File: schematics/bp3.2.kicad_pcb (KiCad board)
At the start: 2 copper layers, 69.5 x 25 mm, 56 parts, among them J1 PowerInput, J2 PowerPassThru, J3 OutputPins, U1 INA128, U2 INA128, U3 INA128, U4 INA128

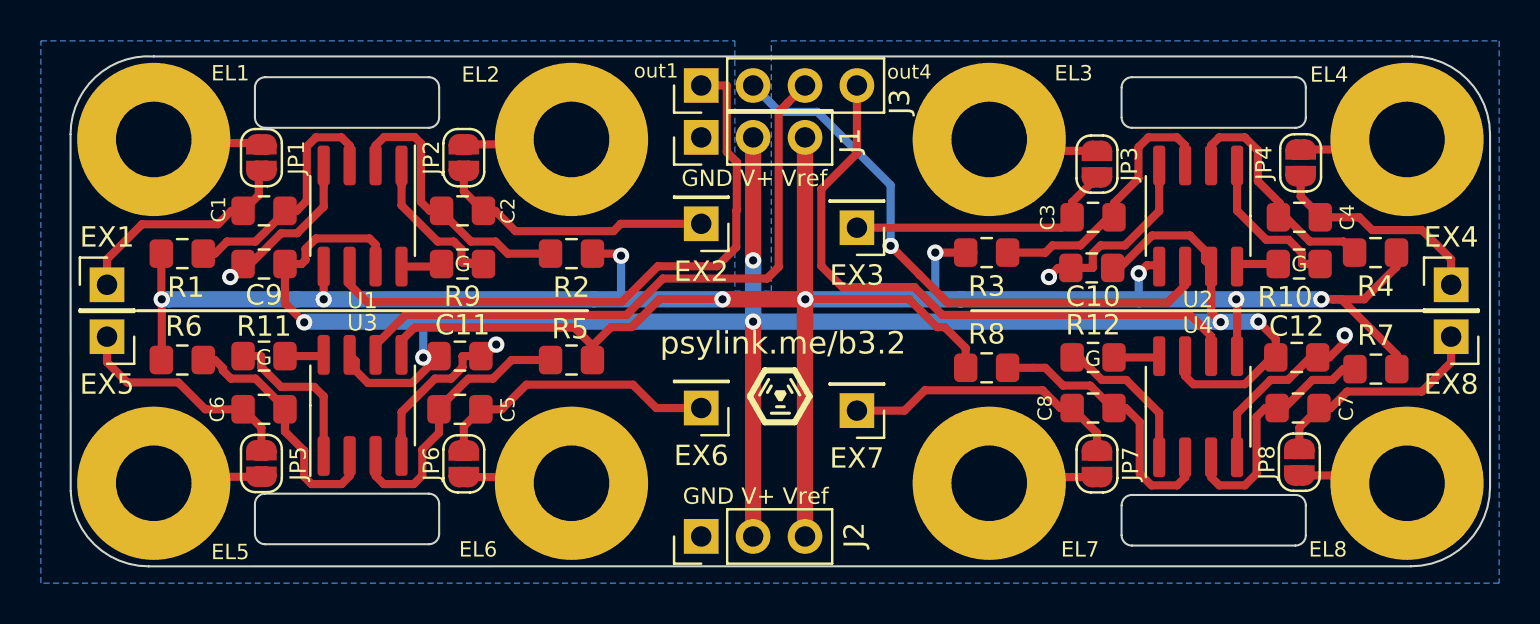
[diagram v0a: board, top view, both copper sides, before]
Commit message: draw rectangles around gain resistors
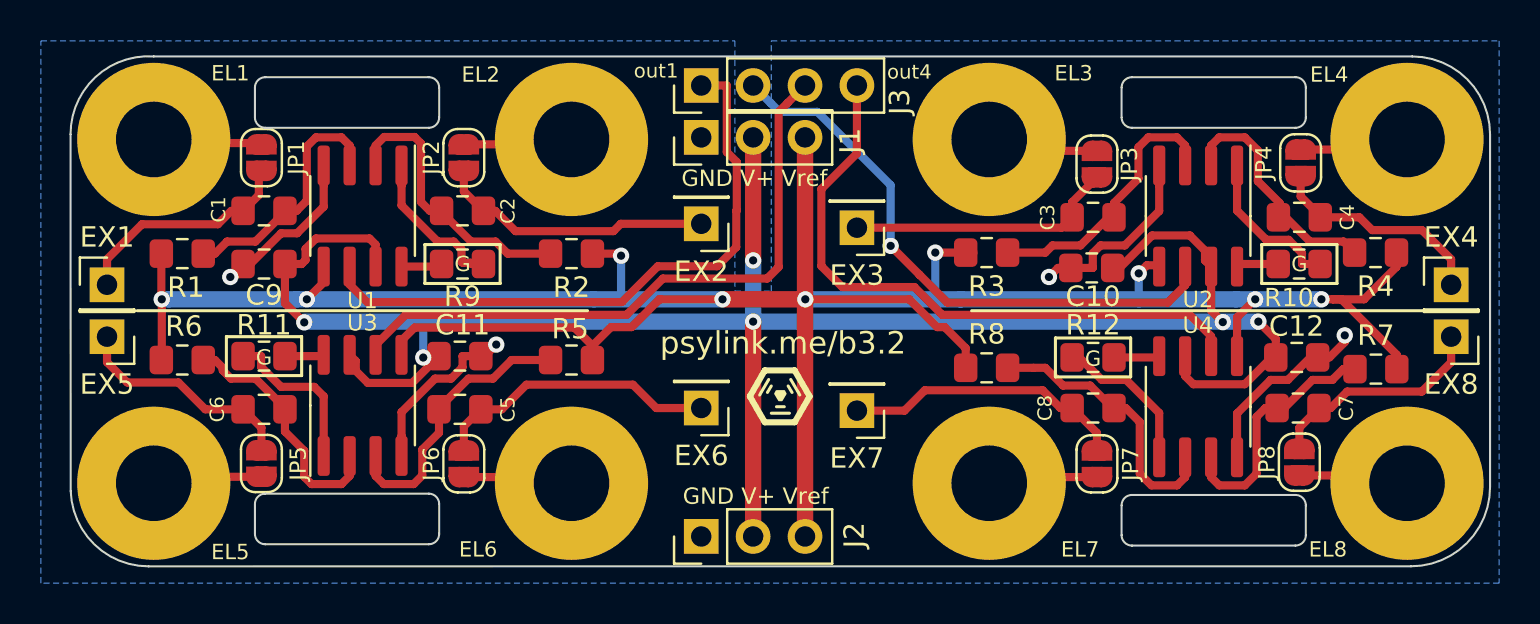
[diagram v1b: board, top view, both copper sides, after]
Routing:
- net GNDS: track 134.4 -> 135.0 mm
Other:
- board text added: "rectangles indicate gain resistors"
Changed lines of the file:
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@@
   (general
     (thickness 1.6)
-    (drawings 70)
-    (tracks 397)
+    (drawings 91)
+    (tracks 398)
     (zones 0)
     (modules 56)
@@
     (tags "resistor handsolder")
     (attr smd)
-    (fp_text reference R10 (at 0.6895 -1.6129) (layer F.SilkS)
-      (effects (font (size 1 1) (thickness 0.15)))
+    (fp_text reference R10 (at 0.499 -1.651) (layer F.SilkS)
+      (effects (font (size 0.9 0.9) (thickness 0.15)))
     )
     (fp_text value 1K/1% (at 0 1.65) (layer F.Fab)
@@
     (tags "resistor handsolder")
     (attr smd)
-    (fp_text reference R11 (at 0 -1.4605 180) (layer F.SilkS)
+    (fp_text reference R11 (at 0 -1.524 180) (layer F.SilkS)
       (effects (font (size 1 1) (thickness 0.15)))
     )
@@
       ))
   )
+  (gr_line (start 82.4865 35.7505) (end 25.019 41.2115) (layer Cmts.User) (width 0.15))
+  (gr_line (start 72.9615 40.767) (end 25.146 41.5925) (layer Cmts.User) (width 0.15))
+  (gr_line (start 42.545 36.2585) (end 24.0665 40.513) (layer Cmts.User) (width 0.15))
+  (gr_line (start 32.8295 39.8145) (end 23.8125 41.021) (layer Cmts.User) (width 0.15))
+  (gr_text "rectangles\nindicate gain\nresistors" (at 17.8435 42.164) (layer Cmts.User)
+    (effects (font (size 1 1) (thickness 0.15)))
+  )
+  (gr_line (start 83.693 34.6075) (end 87.376 34.6075) (layer F.SilkS) (width 0.15))
+  (gr_line (start 87.376 36.5125) (end 83.693 36.5125) (layer F.SilkS) (width 0.15))
+  (gr_line (start 83.693 36.5125) (end 83.693 34.6075) (layer F.SilkS) (width 0.15))
+  (gr_line (start 87.376 34.6075) (end 87.376 36.5125) (layer F.SilkS) (width 0.15))
+  (gr_line (start 73.5965 39.1795) (end 77.2795 39.1795) (layer F.SilkS) (width 0.15))
+  (gr_line (start 77.2795 41.0845) (end 73.5965 41.0845) (layer F.SilkS) (width 0.15))
+  (gr_line (start 73.5965 41.0845) (end 73.5965 39.1795) (layer F.SilkS) (width 0.15))
+  (gr_line (start 77.2795 39.1795) (end 77.2795 41.0845) (layer F.SilkS) (width 0.15))
+  (gr_line (start 42.7355 34.6075) (end 46.4185 34.6075) (layer F.SilkS) (width 0.15))
+  (gr_line (start 46.4185 36.5125) (end 42.7355 36.5125) (layer F.SilkS) (width 0.15))
+  (gr_line (start 42.7355 36.5125) (end 42.7355 34.6075) (layer F.SilkS) (width 0.15))
+  (gr_line (start 46.4185 34.6075) (end 46.4185 36.5125) (layer F.SilkS) (width 0.15))
+  (gr_line (start 33.02 41.021) (end 33.02 39.116) (layer F.SilkS) (width 0.15))
+  (gr_line (start 36.703 41.021) (end 33.02 41.021) (layer F.SilkS) (width 0.15))
+  (gr_line (start 36.703 39.116) (end 36.703 41.021) (layer F.SilkS) (width 0.15))
+  (gr_line (start 33.02 39.116) (end 36.703 39.116) (layer F.SilkS) (width 0.15))
   (gr_line (start 59.69 42.8625) (end 60.579 42.8625) (layer F.SilkS) (width 0.15))
   (gr_line (start 59.944 42.545) (end 60.325 42.545) (layer F.SilkS) (width 0.15))
@@
   (gr_line (start 60.833 40.767) (end 61.563678 42.030839) (layer F.SilkS) (width 0.3))
   (gr_line (start 59.3725 40.767) (end 60.833 40.767) (layer F.SilkS) (width 0.3))
-  (gr_text "This hole in\nthe fill area\nbreaks the\nground loop" (at 19.304 34.3027) (layer Cmts.User)
+  (gr_text "This hole in\nthe fill area\nbreaks the\nground loop" (at 59.055 20.701) (layer Cmts.User)
     (effects (font (size 1 1) (thickness 0.15)))
   )
@@
   (segment (start 58.801 29.3624) (end 58.8264 29.3624) (width 0.8) (layer B.Cu) (net 18))
   (segment (start 58.801 38.3794) (end 58.801 38.3794) (width 0.8) (layer B.Cu) (net 18))
-  (segment (start 81.2165 35.622) (end 81.2165 37.9349) (width 0.4) (layer F.Cu) (net 18))
-  (segment (start 81.2165 37.9349) (end 81.6864 38.4048) (width 0.4) (layer F.Cu) (net 18))
-  (via (at 81.6864 38.4048) (size 0.8) (drill 0.4) (layers F.Cu B.Cu) (net 18))
+  (via (at 81.788 38.4048) (size 0.8) (drill 0.4) (layers F.Cu B.Cu) (net 18))
   (segment (start 58.801 38.3794) (end 45.6184 38.3794) (width 0.8) (layer B.Cu) (net 18))
   (via (at 58.801 38.3794) (size 0.8) (drill 0.4) (layers F.Cu B.Cu) (net 18))
@@
   (segment (start 84.3825 40.132) (end 84.3825 39.234) (width 0.4) (layer F.Cu) (net 18))
   (segment (start 58.801 38.3794) (end 83.5279 38.3794) (width 0.8) (layer B.Cu) (net 18))
+  (segment (start 81.2165 37.8333) (end 81.788 38.4048) (width 0.4) (layer F.Cu) (net 18))
+  (segment (start 81.2165 35.6855) (end 81.2165 37.8333) (width 0.4) (layer F.Cu) (net 18))
   (segment (start 57.3024 37.2872) (end 57.3024 37.2872) (width 0.8) (layer F.Cu) (net 19))
   (via (at 57.3024 37.2872) (size 0.8) (drill 0.4) (layers F.Cu B.Cu) (net 19))
@@
   (via (at 77.6732 36.0172) (size 0.8) (drill 0.4) (layers F.Cu B.Cu) (net 19))
   (segment (start 82.4484 37.2872) (end 86.614 37.2872) (width 0.8) (layer B.Cu) (net 19))
-  (via (at 82.4484 37.2872) (size 0.8) (drill 0.4) (layers F.Cu B.Cu) (net 19))
-  (segment (start 82.4865 37.3253) (end 82.4484 37.2872) (width 0.4) (layer F.Cu) (net 19))
-  (segment (start 82.4865 40.07) (end 82.4865 37.3253) (width 0.4) (layer F.Cu) (net 19))
+  (via (at 83.3755 37.2872) (size 0.8) (drill 0.4) (layers F.Cu B.Cu) (net 19))
   (segment (start 68.9864 37.2872) (end 77.6732 37.2872) (width 0.8) (layer B.Cu) (net 19))
   (segment (start 77.6732 37.2872) (end 77.6732 36.0172) (width 0.4) (layer B.Cu) (net 19))
   (segment (start 77.6732 37.2872) (end 82.4484 37.2872) (width 0.8) (layer B.Cu) (net 19))
-  (segment (start 37.7825 35.622) (end 37.7825 37.2872) (width 0.4) (layer F.Cu) (net 19))
-  (via (at 37.7825 37.2872) (size 0.8) (drill 0.4) (layers F.Cu B.Cu) (net 19))
+  (via (at 36.957 37.2872) (size 0.8) (drill 0.4) (layers F.Cu B.Cu) (net 19))
   (segment (start 61.341 29.3624) (end 61.341 48.895) (width 0.8) (layer F.Cu) (net 19))
   (segment (start 61.3537 37.2872) (end 66.4464 37.2872) (width 0.4) (layer F.Cu) (net 19))
@@
   (segment (start 52.2351 35.052) (end 52.3367 35.1536) (width 0.4) (layer F.Cu) (net 19))
   (segment (start 50.936 35.052) (end 52.2351 35.052) (width 0.4) (layer F.Cu) (net 19))
+  (segment (start 37.7825 36.4617) (end 36.957 37.2872) (width 0.4) (layer F.Cu) (net 19))
+  (segment (start 37.7825 35.6855) (end 37.7825 36.4617) (width 0.4) (layer F.Cu) (net 19))
+  (segment (start 82.4865 38.1762) (end 83.3755 37.2872) (width 0.4) (layer F.Cu) (net 19))
+  (segment (start 82.4865 40.07) (end 82.4865 38.1762) (width 0.4) (layer F.Cu) (net 19))
   (segment (start 57.511001 30.079001) (end 57.511 26.8224) (width 0.4) (layer F.Cu) (net 20))
   (segment (start 57.511 26.8224) (end 56.261 26.8224) (width 0.4) (layer F.Cu) (net 20))

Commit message: hide U* labels under chips. add "signal*" labels.
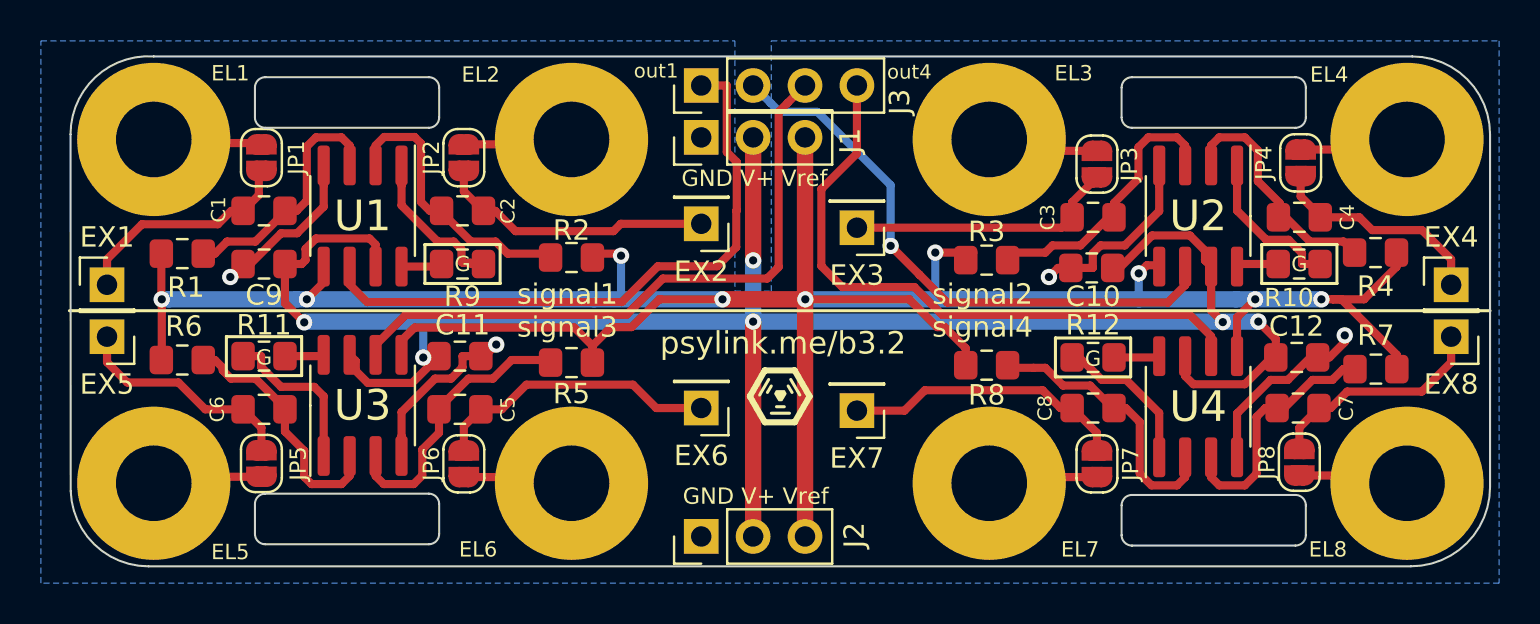
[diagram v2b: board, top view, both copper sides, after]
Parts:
- moved R3 0.37 mm to (70.2, 35.4)
- moved R2 0.19 mm to (49.9, 35.2)
- moved R5 0.13 mm to (49.9, 40.4)
- moved R8 0.13 mm to (70.2, 40.5)
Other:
- board text added: "signal1 signal3"
- board text added: "signal2 signal4"

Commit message: grow INA128's solder pads for easier assembly
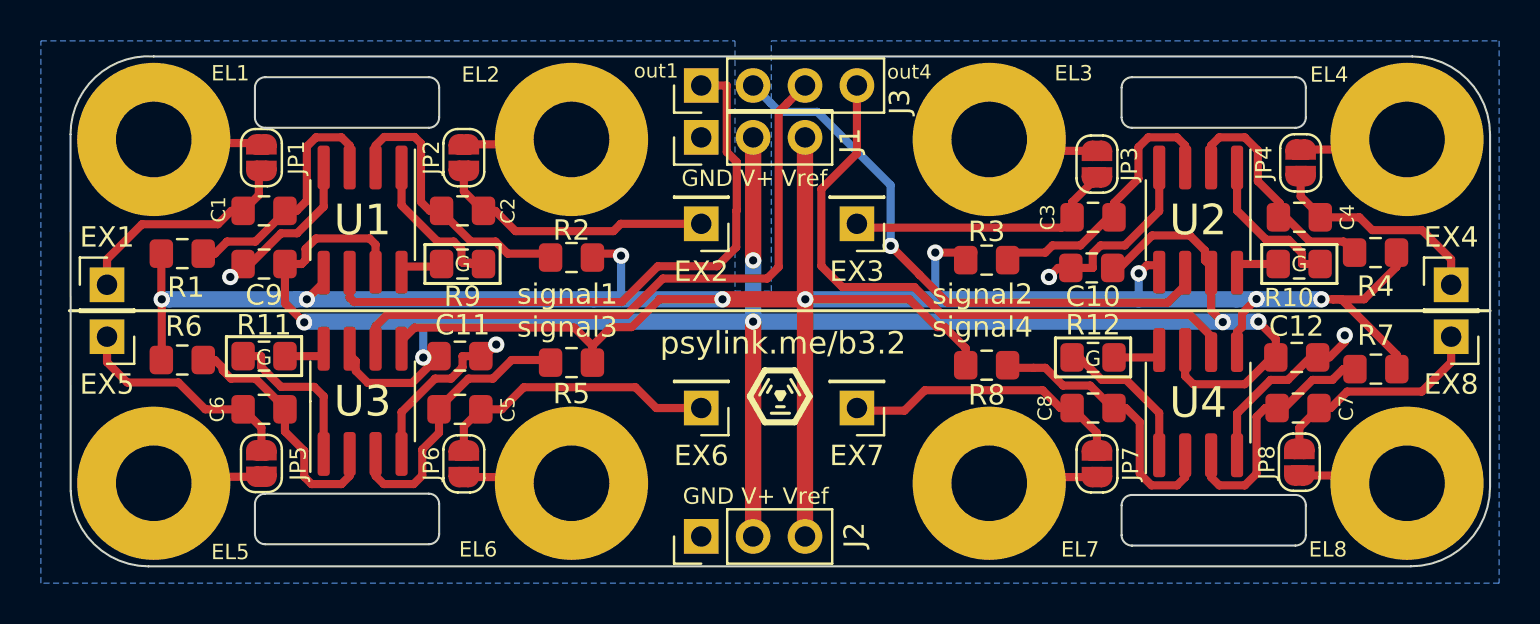
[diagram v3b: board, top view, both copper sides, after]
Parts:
- moved U4 0.20 mm to (80.6, 42.3)
- moved U1 0.20 mm to (39.7, 33.4)
- moved U2 0.20 mm to (80.6, 33.4)
- moved U3 0.20 mm to (39.7, 42.3)
- moved EX3 0.19 mm to (63.9, 33.6)
- moved EX7 0.13 mm to (63.9, 42.6)
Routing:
- net /out1: track 30.8 -> 31.8 mm
- net /out3: track 31.2 -> 32.0 mm

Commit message: tweak silkscreen
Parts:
- J1, J2, J3: moved to B.Cu
- turned J1 to 270 degrees
- turned J2 to 270 degrees
- turned J3 to 270 degrees

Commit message: add silkscreen on backside for signals and electrode polarity
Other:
- board text added: "+"
- board text added: "-"
- board text added: "signal 1"
- board text added: "signal 2"
- board text added: "signal 3"
- board text added: "signal 4"
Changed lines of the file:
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@@
   (general
     (thickness 1.6)
-    (drawings 92)
+    (drawings 108)
     (tracks 402)
     (zones 0)
@@
       ))
   )
+  (gr_text - (at 49.911 41.402) (layer B.SilkS)
+    (effects (font (size 1 1) (thickness 0.15)) (justify mirror))
+  )
+  (gr_text + (at 70.358 41.402) (layer B.SilkS)
+    (effects (font (size 1 1) (thickness 0.15)) (justify mirror))
+  )
+  (gr_text - (at 90.805 41.402) (layer B.SilkS)
+    (effects (font (size 1 1) (thickness 0.15)) (justify mirror))
+  )
+  (gr_text + (at 29.464 41.402) (layer B.SilkS)
+    (effects (font (size 1 1) (thickness 0.15)) (justify mirror))
+  )
+  (gr_text + (at 90.805 34.163) (layer B.SilkS)
+    (effects (font (size 1 1) (thickness 0.15)) (justify mirror))
+  )
+  (gr_text - (at 70.358 34.163) (layer B.SilkS)
+    (effects (font (size 1 1) (thickness 0.15)) (justify mirror))
+  )
+  (gr_text - (at 29.464 34.163) (layer B.SilkS)
+    (effects (font (size 1 1) (thickness 0.15)) (justify mirror))
+  )
+  (gr_text + (at 49.911 34.163) (layer B.SilkS)
+    (effects (font (size 1 1) (thickness 0.15)) (justify mirror))
+  )
+  (gr_text "signal 4" (at 78.1685 44.1325) (layer B.SilkS)
+    (effects (font (size 1 1) (thickness 0.15)) (justify mirror))
+  )
+  (gr_line (start 73.914 44.831) (end 87.249 44.831) (layer B.SilkS) (width 0.15))
+  (gr_line (start 73.914 30.988) (end 87.249 30.988) (layer B.SilkS) (width 0.15))
+  (gr_text "signal 2" (at 78.1685 30.2895) (layer B.SilkS)
+    (effects (font (size 1 1) (thickness 0.15)) (justify mirror))
+  )
+  (gr_line (start 33.02 44.831) (end 46.355 44.831) (layer B.SilkS) (width 0.15))
+  (gr_text "signal 3" (at 37.2745 44.1325) (layer B.SilkS)
+    (effects (font (size 1 1) (thickness 0.15)) (justify mirror))
+  )
+  (gr_line (start 33.02 30.988) (end 46.355 30.988) (layer B.SilkS) (width 0.15))
+  (gr_text "signal 1" (at 37.2745 30.2895) (layer B.SilkS)
+    (effects (font (size 1 1) (thickness 0.15)) (justify mirror))
+  )
   (gr_text "signal1\nsignal3" (at 47.244 37.846) (layer F.SilkS)

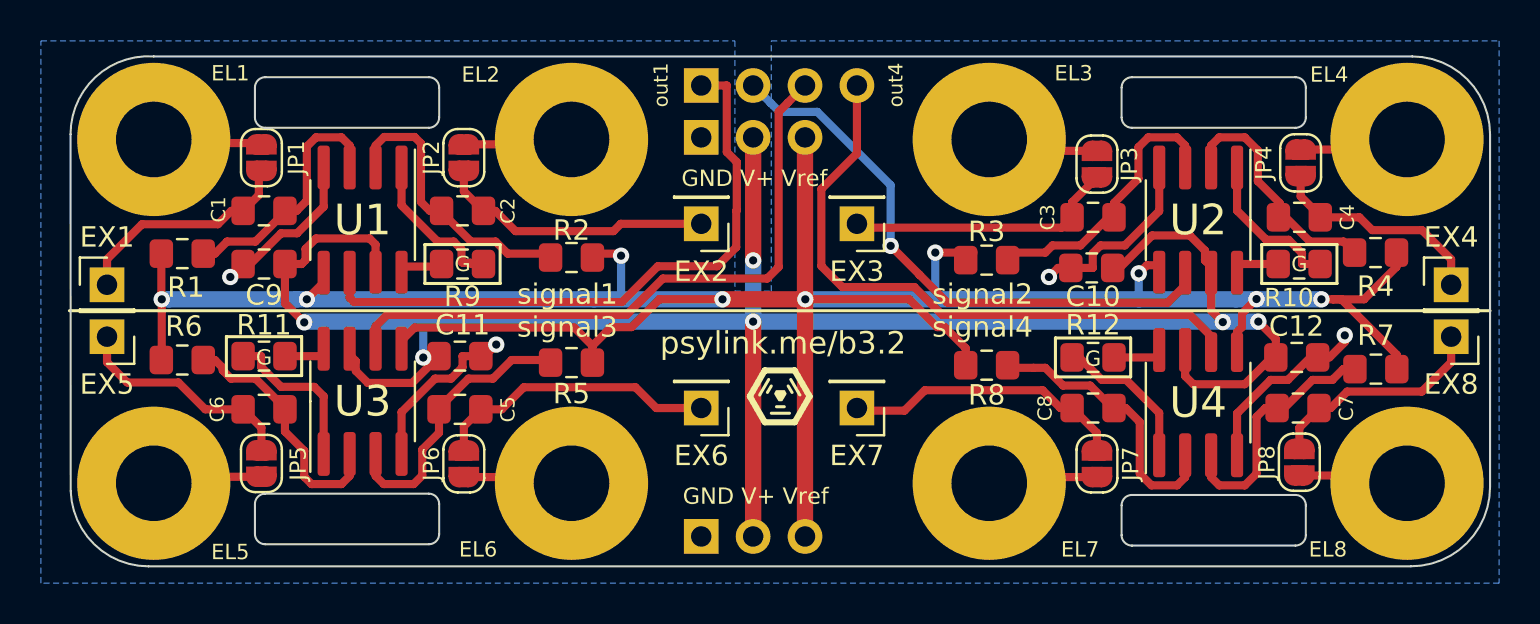
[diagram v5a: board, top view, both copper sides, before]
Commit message: upgrade from c10.1 to c10.2 (bridge solder jumpers by default)
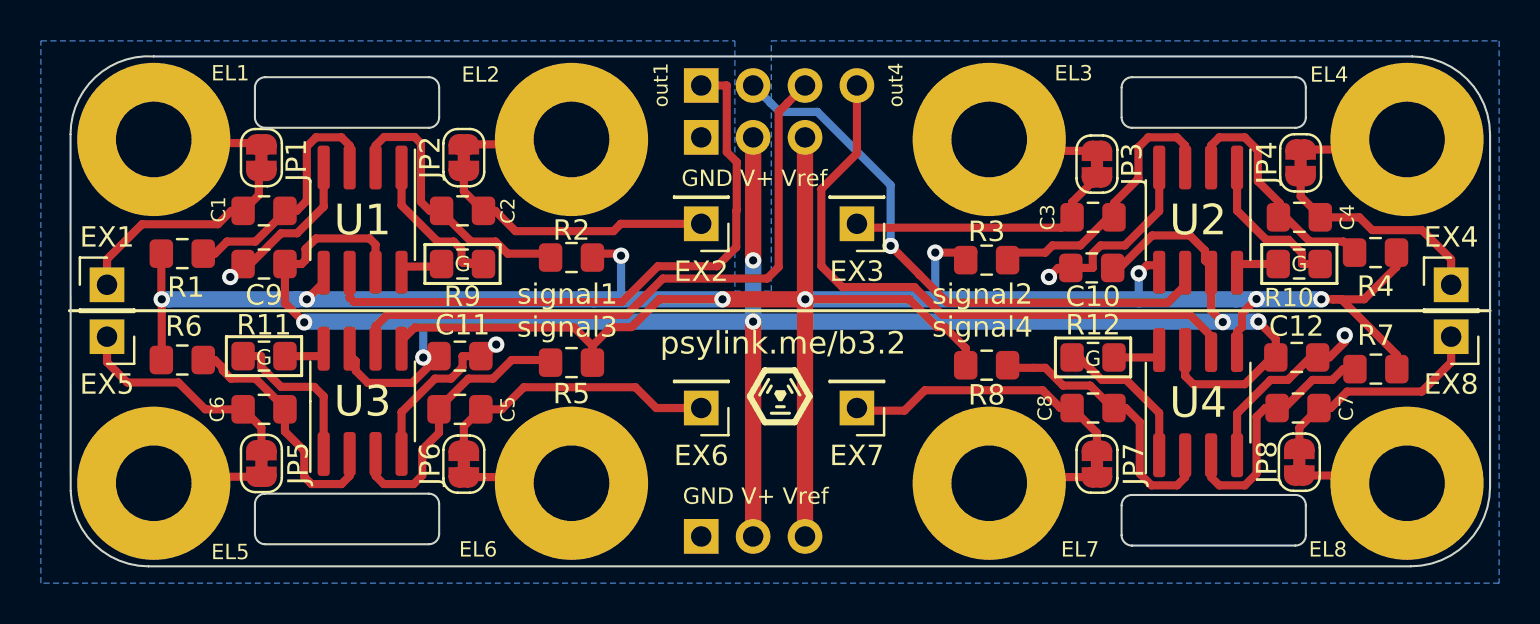
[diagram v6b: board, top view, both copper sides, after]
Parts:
- JP1, JP2, JP3, JP4, JP5, JP6, JP7, JP8: value Jumper_NO_Small -> SolderJumper_2_Bridged; footprint Jumper:SolderJumper-2_P1.3mm_Open_RoundedPad1.0x1.5mm -> Jumper:SolderJumper-2_P1.3mm_Bridged_RoundedPad1.0x1.5mm
- R10, R11, R12, R9: value 1K/1% -> 100/1%
